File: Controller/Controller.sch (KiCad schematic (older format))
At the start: 21 parts, among them P3 MOUNT, P4 MOUNT, P5 MOUNT, P6 MOUNT, P7 MOUNT, Q1 DMN2050L, U1 MDBT40-P, U2 TPS61221, X1 32.768kHz

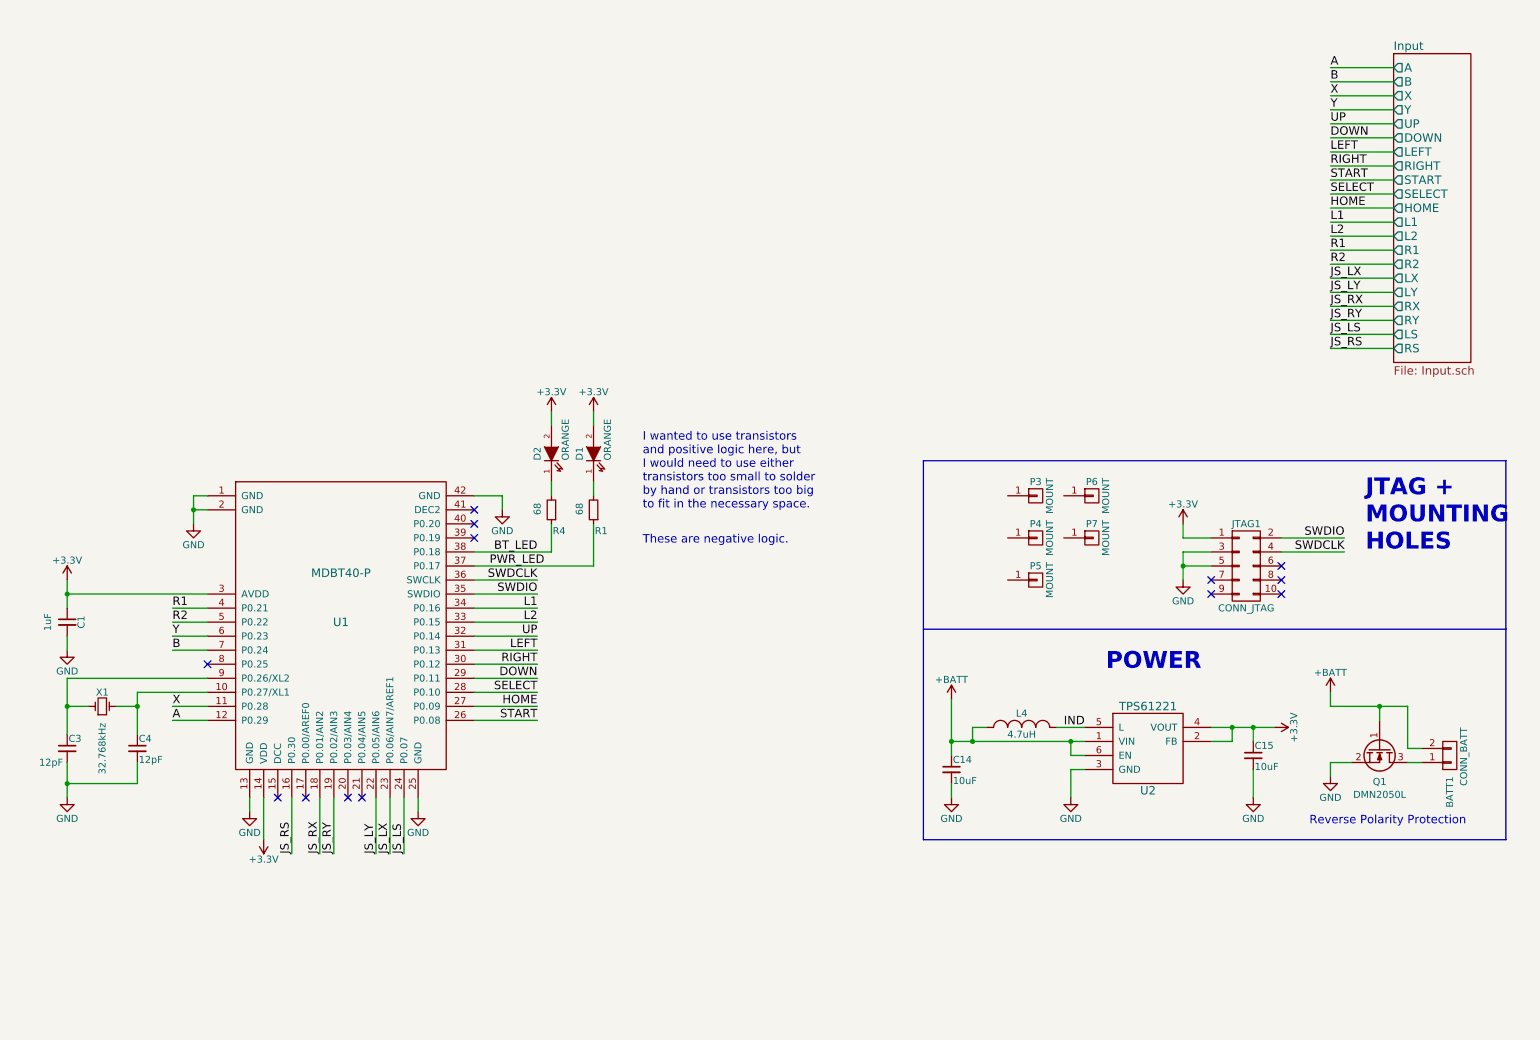
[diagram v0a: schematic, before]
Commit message: Improved traces in power supply circuit. Added clearance on inside of drill holes. Removed sharp inside corners and replaced with cirular cutouts. Removed removed pull-down resistors because I am using internal pull-ups and negative logic with buttons.
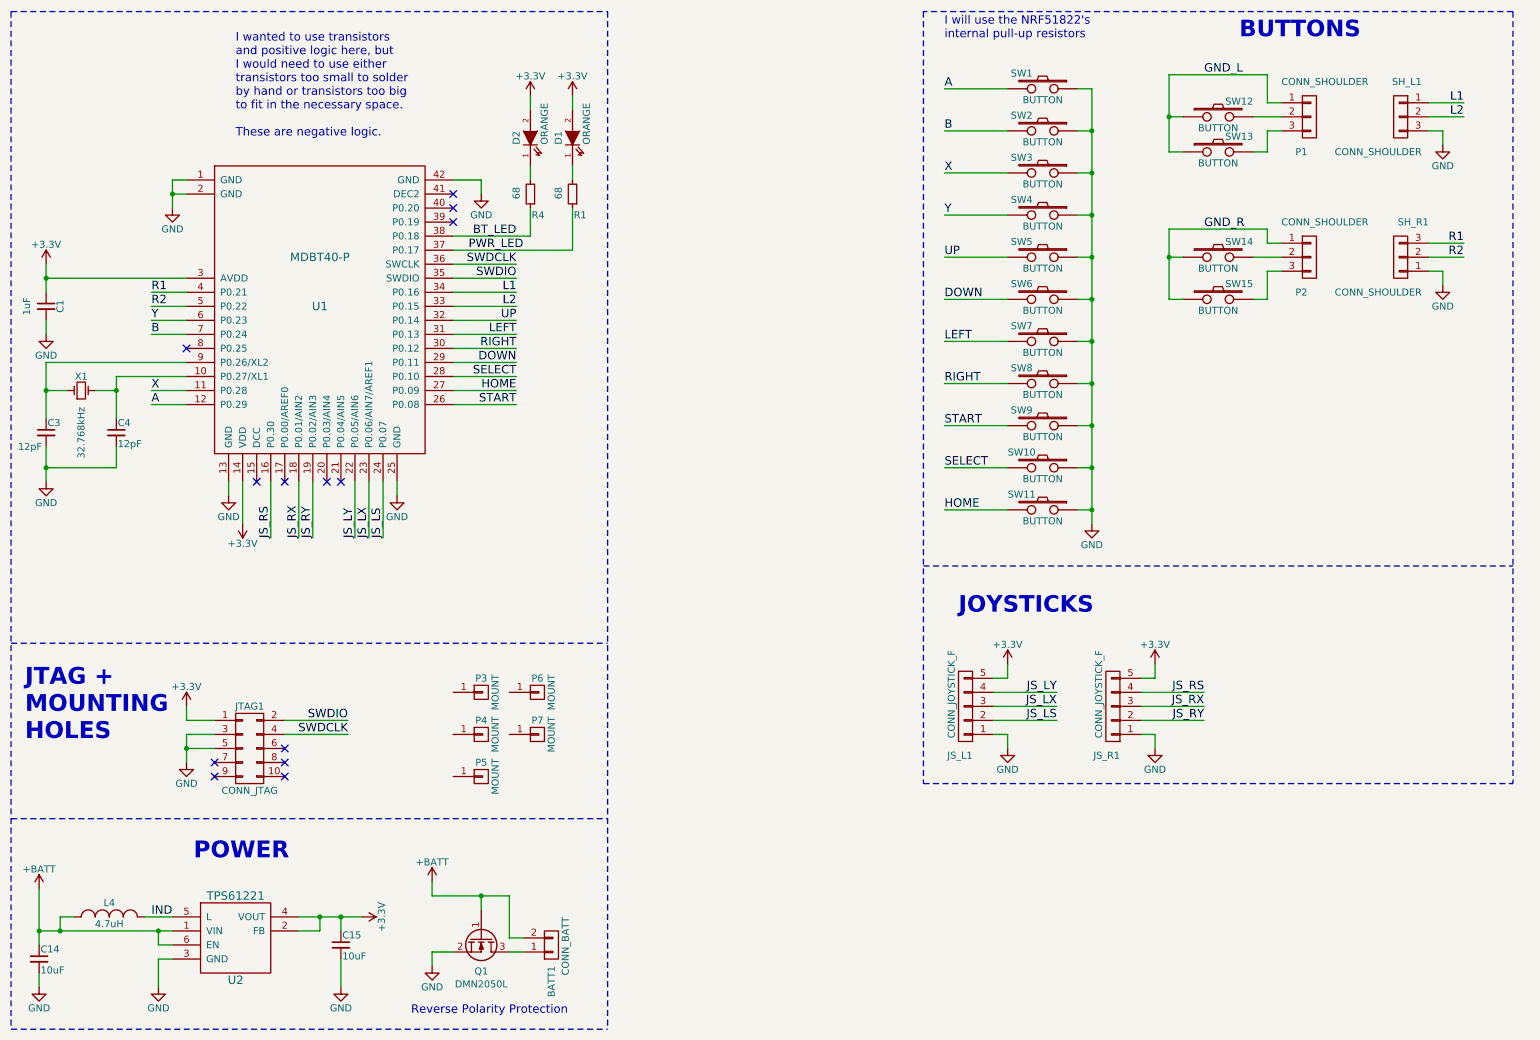
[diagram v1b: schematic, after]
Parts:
- added JS_L1, JS_R1: CONN_JOYSTICK_F, Controller:CONN_JOYSTICK, symbol CONN_JOYSTICK_F
- added P1, P2: CONN_SHOULDER, Controller:CONN_SHOULDER_M, symbol CONN_SHOULDER
- added SH_L1, SH_R1: CONN_SHOULDER, Controller:CONN_SHOULDER_F, symbol CONN_SHOULDER
- added SW1, SW10, SW11, SW12, SW13, SW14, SW15, SW2, SW3, SW4, SW5, SW6, SW7, SW8, SW9: BUTTON, Controller:SW_BUTTON, symbol BUTTON
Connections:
- net +3V3: now also JS_L1.5 (P5), JS_R1.5 (P5)
- net A: now also SW1.2
- net B: now also SW2.2
- net DOWN: now also SW6.2
- net GND: now also JS_L1.1 (P1), JS_R1.1 (P1), SH_L1.3 (P3), SH_R1.1 (P1), SW1.1, SW10.1, SW11.1, SW2.1, SW3.1, SW4.1, SW5.1, SW6.1, SW7.1, SW8.1, SW9.1
- net HOME: now also SW11.2
- net JS_LS: now also JS_L1.2 (P2)
- net JS_LX: now also JS_L1.3 (P3)
- net JS_LY: now also JS_L1.4 (P4)
- net JS_RS: now also JS_R1.4 (P4)
- net JS_RX: now also JS_R1.3 (P3)
- net JS_RY: now also JS_R1.2 (P2)
- net L1: now also SH_L1.1 (P1)
- net L2: now also SH_L1.2 (P2)
- net LEFT: now also SW7.2
- net R1: now also SH_R1.3 (P3)
- net R2: now also SH_R1.2 (P2)
- net RIGHT: now also SW8.2
- net SELECT: now also SW10.2
- net START: now also SW9.2
- net UP: now also SW5.2
- net X: now also SW3.2
- net Y: now also SW4.2
- new net: P1.2 (P2), SW12.2
- new net: P1.3 (P3), SW13.2
- new net: P2.2 (P2), SW14.2
- new net: P2.3 (P3), SW15.2
- new net GND_L: P1.1 (P1), SW12.1, SW13.1
- new net GND_R: P2.1 (P1), SW14.1, SW15.1
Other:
- note added: "BUTTONS"
- note added: "I wanted to use transistors\nand positive logic here, but \nI would need to use either\ntransistors too small to solder\nby hand or transistors too big\nto fit in the necessary space.\n\nThese are negative logic."
- note added: "I will use the NRF51822's\ninternal pull-up resistors"
- note added: "JOYSTICKS"
- note removed: "I wanted to use transistors\nand positive logic here, but \nI would need to use either\ntransistors too small to solder\nby hand or transistors too big\nto fit in the necessary space."
- note removed: "These are negative logic."
- moved on the sheet: BATT1, C1, C14, C15, C3, C4, D1, D2, JTAG1, L4, P3, P4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
